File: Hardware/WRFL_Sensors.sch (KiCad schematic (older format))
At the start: 15 parts, among them P10 TEST_POINT, P11 TEST_POINT, P12 JST_XH_8, P9 TEST_POINT, U5 TPS73633DBV, U6 MS5611-01BA03

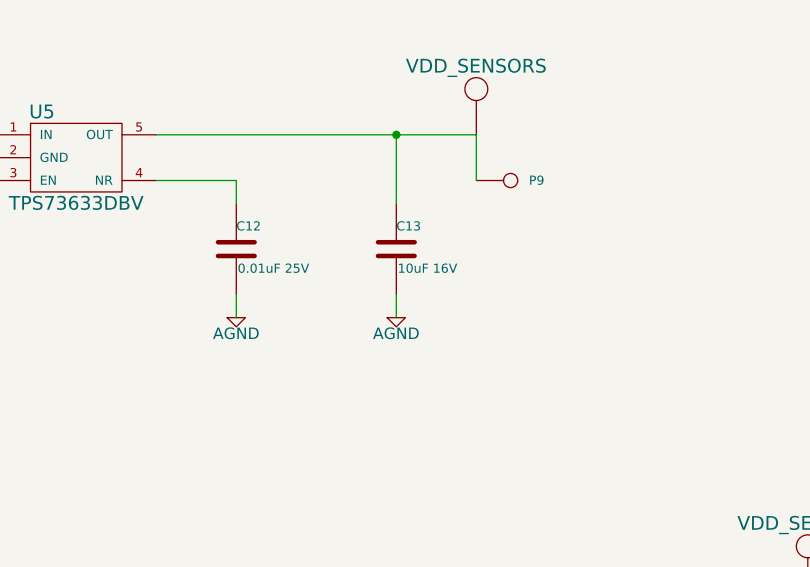
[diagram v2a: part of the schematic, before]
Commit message: added footprint values for caps and resistors
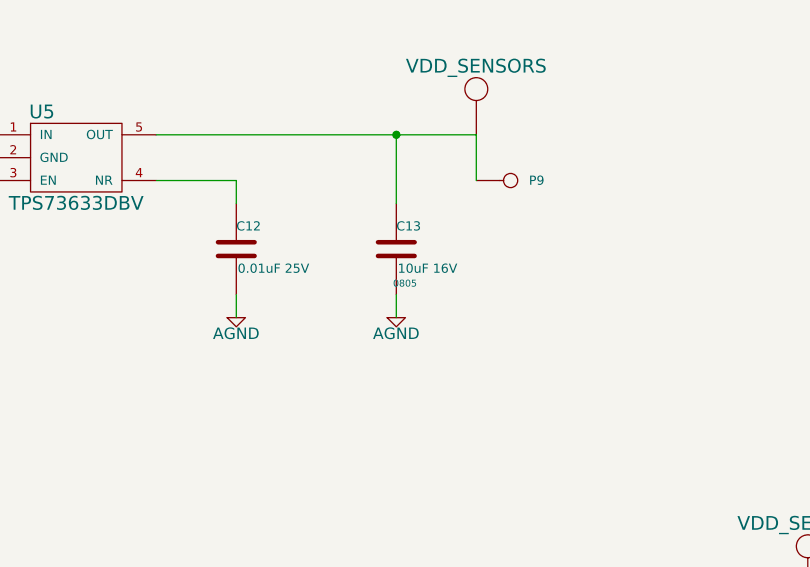
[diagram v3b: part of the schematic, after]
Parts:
- C10, C11, C12, C13, C14, R10, R11, R12, R13: footprint ~ -> 0805
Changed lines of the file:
@@
-EESchema Schematic File Version 2  date Monday, October 07, 2013 09:14:17 AM
+EESchema Schematic File Version 2  date Monday, October 07, 2013 12:52:48 PM
 LIBS:power
 LIBS:device
@@
 F 0 "C10" H 1000 2350 40  0000 L CNN
 F 1 "1uF 10V" H 1006 2165 40  0000 L CNN
-F 2 "~" H 1038 2100 30  0000 C CNN
+F 2 "0805" H 1038 2100 30  0001 C CNN
 F 3 "~" H 1000 2250 60  0000 C CNN
 	1    1000 2250
@@
 F 0 "R11" V 1930 2500 40  0000 C CNN
 F 1 "0Ohm" V 1857 2501 40  0000 C CNN
-F 2 "~" V 1780 2500 30  0000 C CNN
+F 2 "0805" V 1780 2500 30  0001 C CNN
 F 3 "~" H 1850 2500 30  0000 C CNN
 	1    1850 2500
@@
 F 0 "C13" H 4100 2600 40  0000 L CNN
 F 1 "10uF 16V" H 4106 2415 40  0000 L CNN
-F 2 "~" H 4138 2350 30  0000 C CNN
+F 2 "0805" H 4138 2350 30  0000 C CNN
 F 3 "~" H 4100 2500 60  0000 C CNN
 	1    4100 2500
@@
 F 0 "C12" H 3400 2600 40  0000 L CNN
 F 1 "0.01uF 25V" H 3406 2415 40  0000 L CNN
-F 2 "~" H 3438 2350 30  0000 C CNN
+F 2 "0805" H 3438 2350 30  0001 C CNN
 F 3 "~" H 3400 2500 60  0000 C CNN
 	1    3400 2500
@@
 F 0 "R10" V 1830 5050 40  0000 C CNN
 F 1 "100k" V 1757 5051 40  0000 C CNN
-F 2 "~" V 1680 5050 30  0000 C CNN
+F 2 "0805" V 1680 5050 30  0001 C CNN
 F 3 "~" H 1750 5050 30  0000 C CNN
 	1    1750 5050
@@
 F 0 "C11" H 1250 5100 40  0000 L CNN
 F 1 "0.47uF 16V" H 1256 4915 40  0000 L CNN
-F 2 "~" H 1288 4850 30  0000 C CNN
+F 2 "0805" H 1288 4850 30  0001 C CNN
 F 3 "~" H 1250 5000 60  0000 C CNN
 	1    1250 5000
@@
 F 0 "C14" H 9650 1900 40  0000 L CNN
 F 1 "1uF 10V" H 9656 1715 40  0000 L CNN
-F 2 "~" H 9688 1650 30  0000 C CNN
+F 2 "0805" H 9688 1650 30  0001 C CNN
 F 3 "~" H 9650 1800 60  0000 C CNN
 	1    9650 1800
@@
 F 0 "R13" V 8780 1900 40  0000 C CNN
 F 1 "100k" V 8707 1901 40  0000 C CNN
-F 2 "~" V 8630 1900 30  0000 C CNN
+F 2 "0805" V 8630 1900 30  0001 C CNN
 F 3 "~" H 8700 1900 30  0000 C CNN
 	1    8700 1900
@@
 F 0 "R12" V 5980 4500 40  0000 C CNN
 F 1 "100k" V 5907 4501 40  0000 C CNN
-F 2 "~" V 5830 4500 30  0000 C CNN
+F 2 "0805" V 5830 4500 30  0001 C CNN
 F 3 "~" H 5900 4500 30  0000 C CNN
 	1    5900 4500

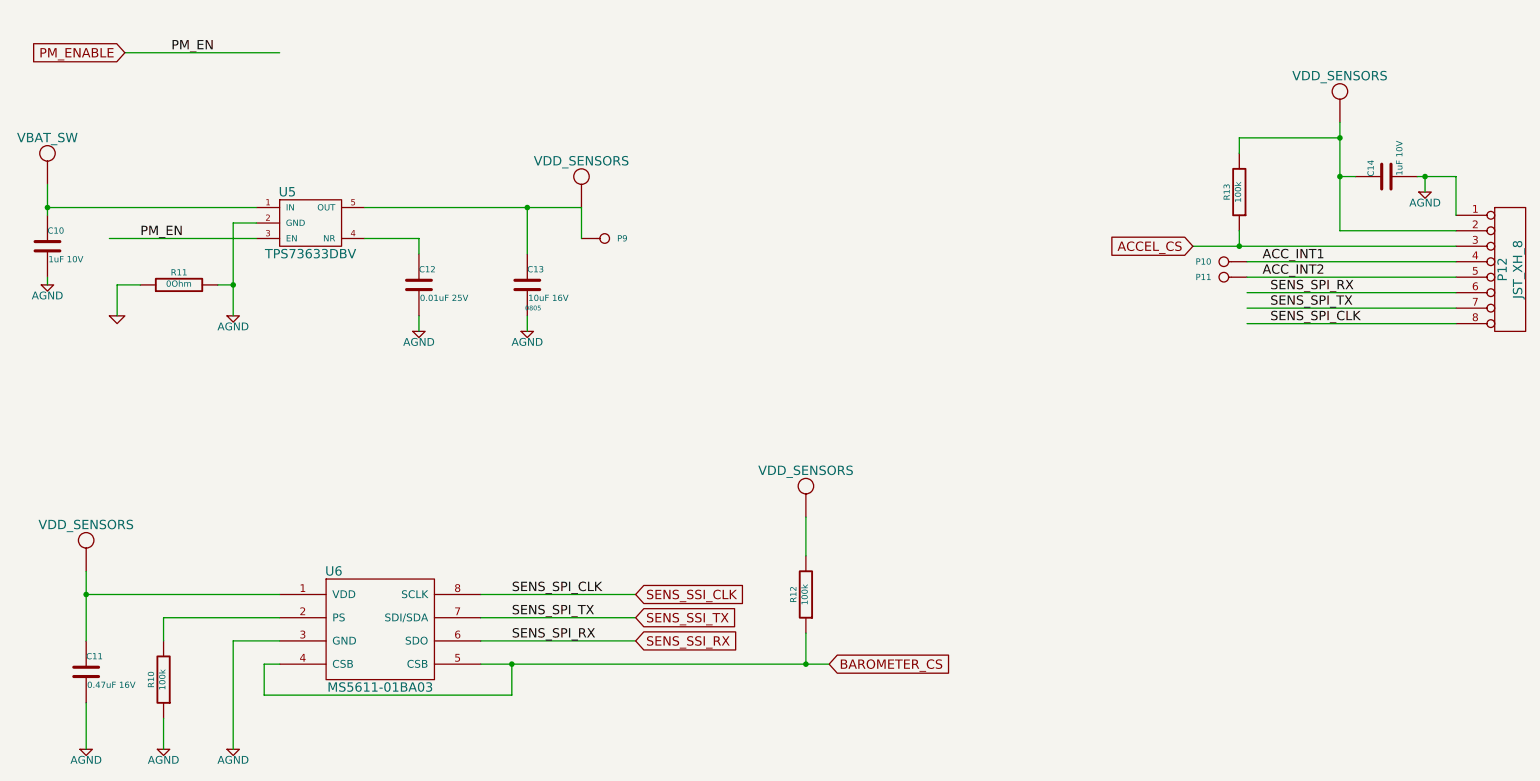
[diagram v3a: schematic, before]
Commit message: Schematics update
Bluetooth sheet added
LCD specific symbol
power management sheet rearrangement
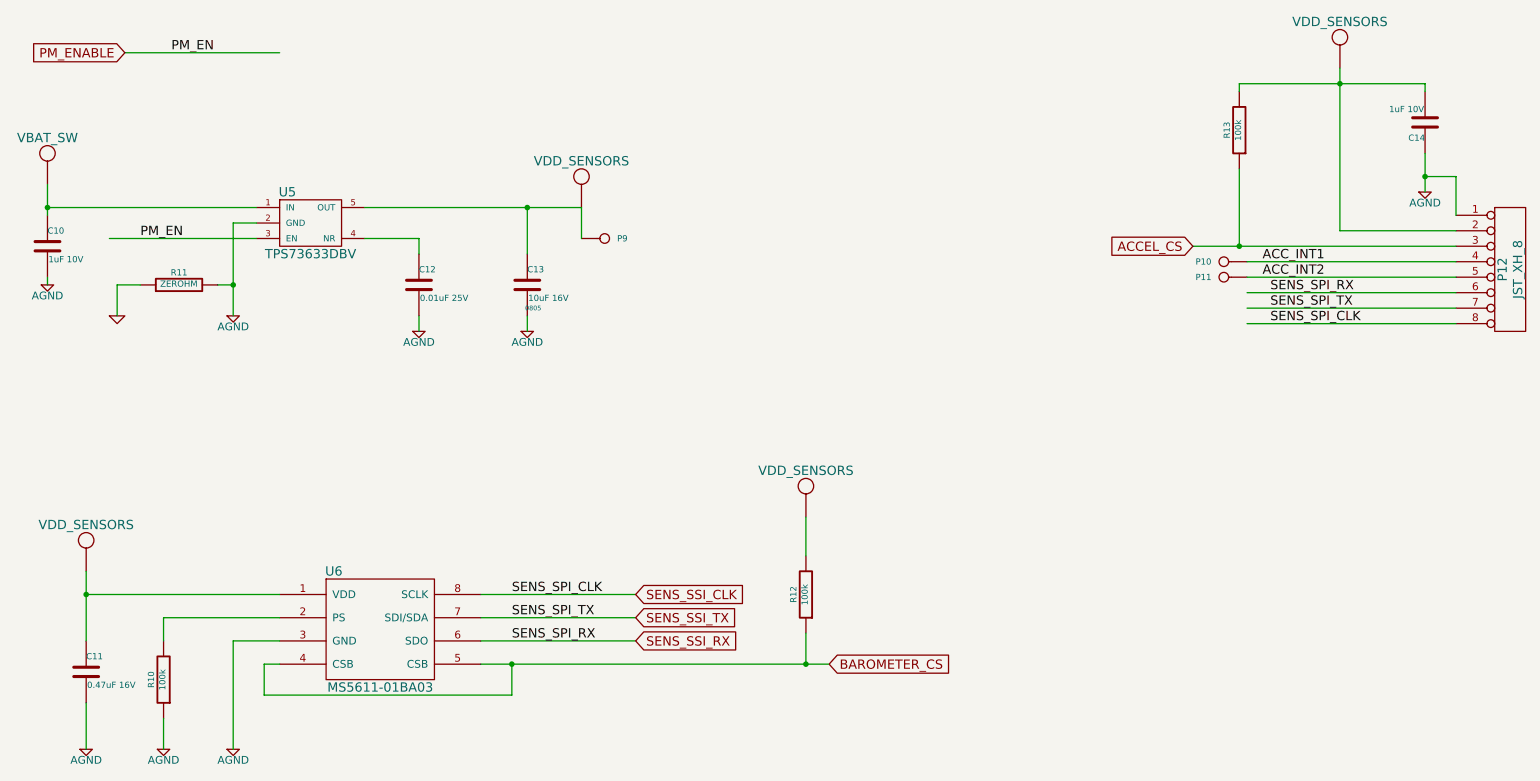
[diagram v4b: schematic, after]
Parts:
- R11: value 0Ohm -> ZEROHM
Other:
- moved on the sheet: C14, R13
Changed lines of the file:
@@
-EESchema Schematic File Version 2  date Monday, October 07, 2013 12:52:48 PM
+EESchema Schematic File Version 2  date 10/11/2013 1:57:23 AM
 LIBS:power
 LIBS:device
@@
 $Descr A4 11693 8268
 encoding utf-8
-Sheet 5 5
+Sheet 5 6
 Title ""
-Date "7 oct 2013"
+Date "10 oct 2013"
 Rev ""
 Comp "Nightmechanic"
@@
 $EndDescr
 $Comp
-L VDD_SENSORS #U17
+L VDD_SENSORS #U20
 U 1 1 524D591B
 P 4450 1800
-F 0 "#U17" H 4450 2000 60  0001 C CNN
+F 0 "#U20" H 4450 2000 60  0001 C CNN
 F 1 "VDD_SENSORS" H 4450 1900 60  0000 C CNN
 F 2 "" H 4450 1800 60  0000 C CNN
@@
 P 1850 2500
 F 0 "R11" V 1930 2500 40  0000 C CNN
-F 1 "0Ohm" V 1857 2501 40  0000 C CNN
+F 1 "ZEROHM" V 1857 2501 40  0000 C CNN
 F 2 "0805" V 1780 2500 30  0001 C CNN
 F 3 "~" H 1850 2500 30  0000 C CNN
@@
 PM_EN
 $Comp
-L VBAT_SW #U15
+L VBAT_SW #U18
 U 1 1 5251CA9A
 P 1000 1650
-F 0 "#U15" H 1000 1850 60  0001 C CNN
+F 0 "#U18" H 1000 1850 60  0001 C CNN
 F 1 "VBAT_SW" H 1000 1750 60  0000 C CNN
 F 2 "~" H 1000 1650 60  0000 C CNN
@@
 Connection ~ 1000 2000
 $Comp
-L VDD_SENSORS #U19
+L VDD_SENSORS #U22
 U 1 1 5251CABC
-P 9350 1250
-F 0 "#U19" H 9350 1450 60  0001 C CNN
-F 1 "VDD_SENSORS" H 9350 1350 60  0000 C CNN
-F 2 "~" H 9350 1250 60  0000 C CNN
-F 3 "~" H 9350 1250 60  0000 C CNN
-	1    9350 1250
+P 9350 900
+F 0 "#U22" H 9350 1100 60  0001 C CNN
+F 1 "VDD_SENSORS" H 9350 1000 60  0000 C CNN
+F 2 "~" H 9350 900 60  0000 C CNN
+F 3 "~" H 9350 900 60  0000 C CNN
+	1    9350 900
 	1    0    0    -1
 $EndComp
@@
 $EndComp
 $Comp
-L VDD_SENSORS #U16
+L VDD_SENSORS #U19
 U 1 1 5251D30C
 P 1250 4150
-F 0 "#U16" H 1250 4350 60  0001 C CNN
+F 0 "#U19" H 1250 4350 60  0001 C CNN
 F 1 "VDD_SENSORS" H 1250 4250 60  0000 C CNN
 F 2 "~" H 1250 4150 60  0000 C CNN
@@
 	10100 1800 10100 2050
 Wire Wire Line
-	9900 1800 9900 1900
+	9900 1650 9900 1900
 Wire Wire Line
 	9350 2150 10100 2150
 Wire Wire Line
-	9350 1450 9350 2150
+	9350 1100 9350 2150
 $Comp
 L C C14
 U 1 1 5251D55A
-P 9650 1800
-F 0 "C14" H 9650 1900 40  0000 L CNN
-F 1 "1uF 10V" H 9656 1715 40  0000 L CNN
-F 2 "0805" H 9688 1650 30  0001 C CNN
-F 3 "~" H 9650 1800 60  0000 C CNN
-	1    9650 1800
-	0    -1   -1   0
-$EndComp
-Wire Wire Line
-	9850 1800 10100 1800
-Connection ~ 9900 1800
-Wire Wire Line
-	9450 1800 9350 1800
-Connection ~ 9350 1800
+P 9900 1450
+F 0 "C14" H 9900 1550 40  0000 L CNN
+F 1 "1uF 10V" H 9906 1365 40  0000 L CNN
+F 2 "0805" H 9938 1300 30  0001 C CNN
+F 3 "~" H 9900 1450 60  0000 C CNN
+	1    9900 1450
+	-1   0    0    1
+$EndComp
 $Comp
 L CONN_1 P9
@@
 L R R13
 U 1 1 5251D93B
-P 8700 1900
-F 0 "R13" V 8780 1900 40  0000 C CNN
-F 1 "100k" V 8707 1901 40  0000 C CNN
-F 2 "0805" V 8630 1900 30  0001 C CNN
-F 3 "~" H 8700 1900 30  0000 C CNN
-	1    8700 1900
+P 8700 1500
+F 0 "R13" V 8780 1500 40  0000 C CNN
+F 1 "100k" V 8707 1501 40  0000 C CNN
+F 2 "0805" V 8630 1500 30  0001 C CNN
+F 3 "~" H 8700 1500 30  0000 C CNN
+	1    8700 1500
 	-1   0    0    1
 $EndComp
 Wire Wire Line
-	8700 1650 8700 1550
-Wire Wire Line
-	8700 1550 9350 1550
-Connection ~ 9350 1550
-Wire Wire Line
-	8700 2150 8700 2250
+	8700 1250 8700 1200
+Wire Wire Line
+	8700 1200 9900 1200
+Connection ~ 9350 1200
+Wire Wire Line
+	8700 1750 8700 2250
 Connection ~ 8700 2250
 $Comp
@@
 $EndComp
 $Comp
-L VDD_SENSORS #U18
+L VDD_SENSORS #U21
 U 1 1 5251D9FD
 P 5900 3800
-F 0 "#U18" H 5900 4000 60  0001 C CNN
+F 0 "#U21" H 5900 4000 60  0001 C CNN
 F 1 "VDD_SENSORS" H 5900 3900 60  0000 C CNN
 F 2 "~" H 5900 3800 60  0000 C CNN
@@
 	1    0    0    -1
 $EndComp
+Wire Wire Line
+	9900 1200 9900 1250
+Wire Wire Line
+	10100 1800 9900 1800
+Connection ~ 9900 1800
 $EndSCHEMATC
